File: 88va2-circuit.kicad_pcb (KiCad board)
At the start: 4 copper layers, 380 x 237.5 mm, 52 parts, among them CN2 FDD, CN4 TEXT BUS, CN5 LED, IC1 D65101GD055, IC13 SN74ALS374N, IC20 7407, IC21 uPD4990AC, IC22 DIP-14_W7.62mm, IC65 D65101GD110, IC8 SN74ALS374N, IC9 D65200GD076, X2 32.768K

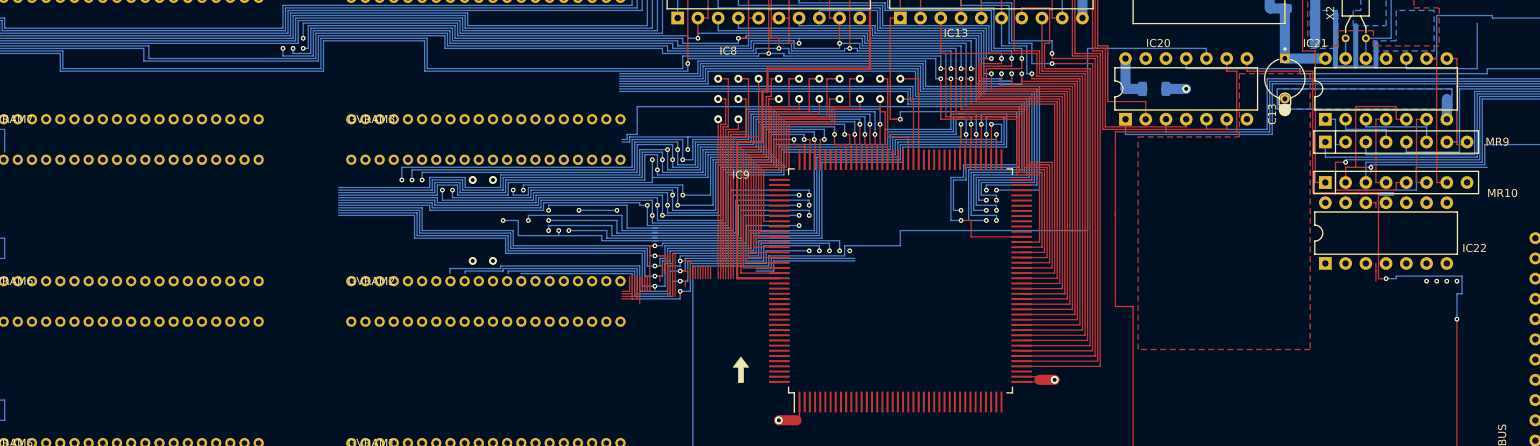
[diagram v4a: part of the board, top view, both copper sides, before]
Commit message: pcb: wire IC9 to GVRAM GA1x
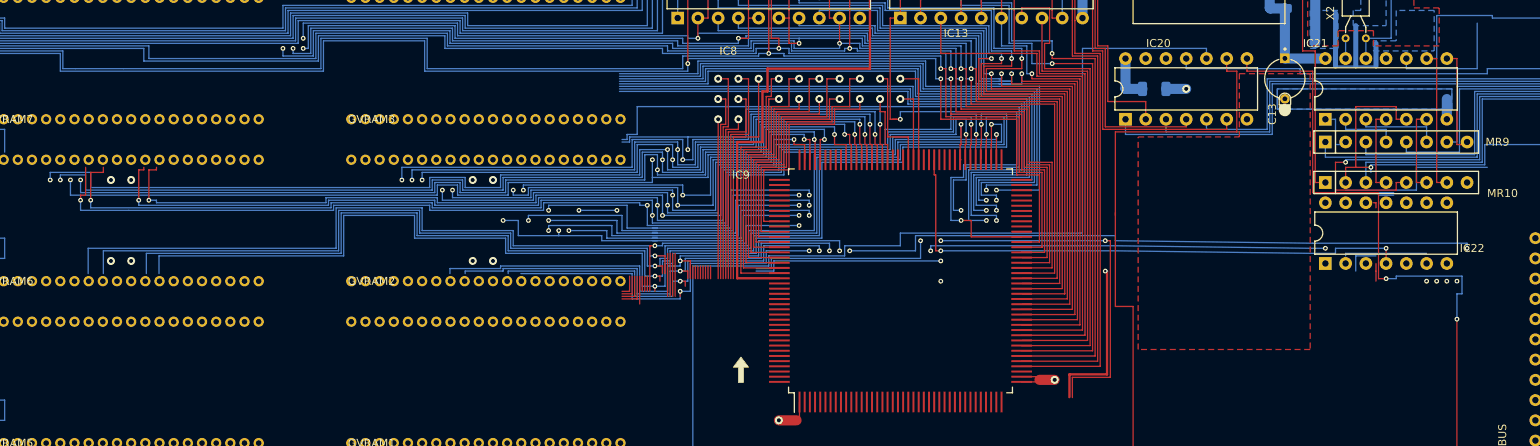
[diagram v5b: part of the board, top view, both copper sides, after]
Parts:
- IC22: value DIP-14_W7.62mm -> SN74LS74N
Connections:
- CN4 pad C1: unconnected-(CN4-??-PadC1) -> (no net)
- CN4 pad C13: (no net) -> GSCLK
- CN4 pad C24: (no net) -> IC9_90
- GVRAM1 pad 39: unconnected-(GVRAM1-~{SOE}-Pad39) -> XSOE
- GVRAM1 pad 40: unconnected-(GVRAM1-~{SEN}-Pad40) -> XSEN1
- GVRAM2 pad 39: unconnected-(GVRAM2-~{SOE}-Pad39) -> XSOE
- GVRAM2 pad 40: unconnected-(GVRAM2-~{SEN}-Pad40) -> XSEN1
- GVRAM3 pad 39: unconnected-(GVRAM3-~{SOE}-Pad39) -> XSOE
- GVRAM3 pad 40: unconnected-(GVRAM3-~{SEN}-Pad40) -> XSEN1
- GVRAM4 pad 39: unconnected-(GVRAM4-~{SOE}-Pad39) -> XSOE
- GVRAM4 pad 40: unconnected-(GVRAM4-~{SEN}-Pad40) -> XSEN1
- GVRAM5 pad 12: unconnected-(GVRAM5-A2-Pad12) -> GA12
- GVRAM5 pad 13: unconnected-(GVRAM5-A3-Pad13) -> GA13
- GVRAM5 pad 14: unconnected-(GVRAM5-~{RAS}-Pad14) -> XGRAS11
- GVRAM5 pad 15: unconnected-(GVRAM5-~{DT}/~{OE}-Pad15) -> XDTOE2
- GVRAM5 pad 26: unconnected-(GVRAM5-~{WE}/~{ME}-Pad26) -> XGWE2
- GVRAM5 pad 27: unconnected-(GVRAM5-~{CAS}-Pad27) -> XGCAS1
- GVRAM5 pad 28: unconnected-(GVRAM5-A4-Pad28) -> GA14
- GVRAM5 pad 29: unconnected-(GVRAM5-A5-Pad29) -> GA15
- GVRAM5 pad 32: unconnected-(GVRAM5-A6-Pad32) -> GA16
- GVRAM5 pad 33: unconnected-(GVRAM5-A7-Pad33) -> GA17
- GVRAM5 pad 39: unconnected-(GVRAM5-~{SOE}-Pad39) -> XSOE
- GVRAM5 pad 40: unconnected-(GVRAM5-~{SEN}-Pad40) -> XSEN2
- GVRAM5 pad 8: unconnected-(GVRAM5-A0-Pad8) -> GA10
- GVRAM5 pad 9: unconnected-(GVRAM5-A1-Pad9) -> GA11
- GVRAM6 pad 12: unconnected-(GVRAM6-A2-Pad12) -> GA12
- GVRAM6 pad 13: unconnected-(GVRAM6-A3-Pad13) -> GA13
- GVRAM6 pad 14: unconnected-(GVRAM6-~{RAS}-Pad14) -> XGRAS11
- GVRAM6 pad 15: unconnected-(GVRAM6-~{DT}/~{OE}-Pad15) -> XDTOE2
- GVRAM6 pad 26: unconnected-(GVRAM6-~{WE}/~{ME}-Pad26) -> XGWE2
- GVRAM6 pad 27: unconnected-(GVRAM6-~{CAS}-Pad27) -> XGCAS1
- GVRAM6 pad 28: unconnected-(GVRAM6-A4-Pad28) -> GA14
- GVRAM6 pad 29: unconnected-(GVRAM6-A5-Pad29) -> GA15
- GVRAM6 pad 32: unconnected-(GVRAM6-A6-Pad32) -> GA16
- GVRAM6 pad 33: unconnected-(GVRAM6-A7-Pad33) -> GA17
- GVRAM6 pad 39: unconnected-(GVRAM6-~{SOE}-Pad39) -> XSOE
- GVRAM6 pad 40: unconnected-(GVRAM6-~{SEN}-Pad40) -> XSEN2
- GVRAM6 pad 8: unconnected-(GVRAM6-A0-Pad8) -> GA10
- GVRAM6 pad 9: unconnected-(GVRAM6-A1-Pad9) -> GA11
- GVRAM7 pad 12: unconnected-(GVRAM7-A2-Pad12) -> GA12
- GVRAM7 pad 13: unconnected-(GVRAM7-A3-Pad13) -> GA13
- GVRAM7 pad 14: unconnected-(GVRAM7-~{RAS}-Pad14) -> XGRAS11
- GVRAM7 pad 15: unconnected-(GVRAM7-~{DT}/~{OE}-Pad15) -> XDTOE3
- GVRAM7 pad 26: unconnected-(GVRAM7-~{WE}/~{ME}-Pad26) -> XGWE3
- GVRAM7 pad 27: unconnected-(GVRAM7-~{CAS}-Pad27) -> XGCAS1
- GVRAM7 pad 28: unconnected-(GVRAM7-A4-Pad28) -> GA14
- GVRAM7 pad 29: unconnected-(GVRAM7-A5-Pad29) -> GA15
- GVRAM7 pad 32: unconnected-(GVRAM7-A6-Pad32) -> GA16
- GVRAM7 pad 33: unconnected-(GVRAM7-A7-Pad33) -> GA17
- GVRAM7 pad 39: unconnected-(GVRAM7-~{SOE}-Pad39) -> XSOE
- GVRAM7 pad 40: unconnected-(GVRAM7-~{SEN}-Pad40) -> XSEN2
- GVRAM7 pad 8: unconnected-(GVRAM7-A0-Pad8) -> GA10
- GVRAM7 pad 9: unconnected-(GVRAM7-A1-Pad9) -> GA11
- GVRAM8 pad 12: unconnected-(GVRAM8-A2-Pad12) -> GA12
- GVRAM8 pad 13: unconnected-(GVRAM8-A3-Pad13) -> GA13
- GVRAM8 pad 14: unconnected-(GVRAM8-~{RAS}-Pad14) -> XGRAS11
- GVRAM8 pad 15: unconnected-(GVRAM8-~{DT}/~{OE}-Pad15) -> XDTOE3
- GVRAM8 pad 26: unconnected-(GVRAM8-~{WE}/~{ME}-Pad26) -> XGWE3
- GVRAM8 pad 27: unconnected-(GVRAM8-~{CAS}-Pad27) -> XGCAS1
- GVRAM8 pad 28: unconnected-(GVRAM8-A4-Pad28) -> GA14
- GVRAM8 pad 29: unconnected-(GVRAM8-A5-Pad29) -> GA15
- GVRAM8 pad 32: unconnected-(GVRAM8-A6-Pad32) -> GA16
- GVRAM8 pad 33: unconnected-(GVRAM8-A7-Pad33) -> GA17
- GVRAM8 pad 39: unconnected-(GVRAM8-~{SOE}-Pad39) -> XSOE
- GVRAM8 pad 40: unconnected-(GVRAM8-~{SEN}-Pad40) -> XSEN2
- GVRAM8 pad 8: unconnected-(GVRAM8-A0-Pad8) -> GA10
- GVRAM8 pad 9: unconnected-(GVRAM8-A1-Pad9) -> GA11
- IC22 pad 1: (no net) -> unconnected-(IC22A-~{R}-Pad1)
- IC22 pad 2: (no net) -> unconnected-(IC22A-D-Pad2)
- IC22 pad 3: (no net) -> unconnected-(IC22A-C-Pad3)
- IC22 pad 4: (no net) -> Net-(IC22A-~{S})
- IC22 pad 5: (no net) -> unconnected-(IC22A-Q-Pad5)
- IC22 pad 6: (no net) -> unconnected-(IC22A-~{Q}-Pad6)
- IC9 pad 112: (no net) -> unconnected-(IC9-GA00-Pad112)
- IC9 pad 113: (no net) -> unconnected-(IC9-GA01-Pad113)
- IC9 pad 114: (no net) -> unconnected-(IC9-GA02-Pad114)
- IC9 pad 115: (no net) -> unconnected-(IC9-GA03-Pad115)
- IC9 pad 116: (no net) -> unconnected-(IC9-GA04-Pad116)
- IC9 pad 117: (no net) -> unconnected-(IC9-GA05-Pad117)
- IC9 pad 118: (no net) -> unconnected-(IC9-GA06-Pad118)
- IC9 pad 119: (no net) -> unconnected-(IC9-GA07-Pad119)
- IC9 pad 123: (no net) -> unconnected-(IC9-XGRAS0-Pad123)
- IC9 pad 124: (no net) -> unconnected-(IC9-XGCAS0-Pad124)
- IC9 pad 125: (no net) -> unconnected-(IC9-XGWE0-Pad125)
- IC9 pad 126: (no net) -> unconnected-(IC9-XGWE1-Pad126)
- IC9 pad 127: (no net) -> unconnected-(IC9-XDT0-Pad127)
- IC9 pad 128: (no net) -> unconnected-(IC9-XDT1-Pad128)
- IC9 pad 130: (no net) -> unconnected-(IC9-GDRQ0-Pad130)
- IC9 pad 155: (no net) -> unconnected-(IC9-XG0BLK-Pad155)
- IC9 pad 156: (no net) -> unconnected-(IC9-XG1BLK-Pad156)
- IC9 pad 43: (no net) -> GSCLK
- IC9 pad 70: (no net) -> XSOE
- IC9 pad 71: (no net) -> XSEN1
- IC9 pad 72: (no net) -> XSEN2
- IC9 pad 73: (no net) -> XDTOE2
- IC9 pad 74: (no net) -> XDTOE3
- IC9 pad 75: (no net) -> XGWE2
- IC9 pad 76: (no net) -> XGWE3
- IC9 pad 77: (no net) -> XGCAS1
- IC9 pad 78: (no net) -> XGRAS11
- IC9 pad 82: (no net) -> GA10
- IC9 pad 83: (no net) -> GA11
- IC9 pad 84: (no net) -> GA12
- IC9 pad 85: (no net) -> GA13
- IC9 pad 86: (no net) -> GA14
- IC9 pad 87: (no net) -> GA15
- IC9 pad 88: (no net) -> GA16
- IC9 pad 89: (no net) -> GA17
- IC9 pad 90: (no net) -> IC9_90
- IC9 pad 94: (no net) -> Net-(IC22A-~{S})
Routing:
- net (no net): track 5921.5 -> 5192.5 mm, vias 122 -> 111
- net GA13: track 0.00 -> 153.7 mm, vias 0 -> 2
- net GA11: track 0.00 -> 153.0 mm, vias 0 -> 2
- net GA12: track 0.00 -> 152.1 mm, vias 0 -> 2
- net GA10: track 0.00 -> 150.2 mm, vias 0 -> 2
- net GA16: track 0.00 -> 139.8 mm, vias 0 -> 3
- net GA17: track 0.00 -> 139.0 mm, vias 0 -> 3
- net GA15: track 0.00 -> 133.4 mm, vias 0 -> 3
- net GA14: track 0.00 -> 132.5 mm, vias 0 -> 3
- net Net-(IC22A-~{S}): track 0.00 -> 70.7 mm, vias 0 -> 2
- net unconnected-(IC9-GA06-Pad118): track 0.00 -> 62.0 mm, vias 0 -> 3
- net unconnected-(IC9-GA07-Pad119): track 0.00 -> 62.0 mm, vias 0 -> 3
- net unconnected-(IC9-GA05-Pad117): track 0.00 -> 54.4 mm, vias 0 -> 3
- net unconnected-(IC9-GA04-Pad116): track 0.00 -> 52.3 mm, vias 0 -> 3

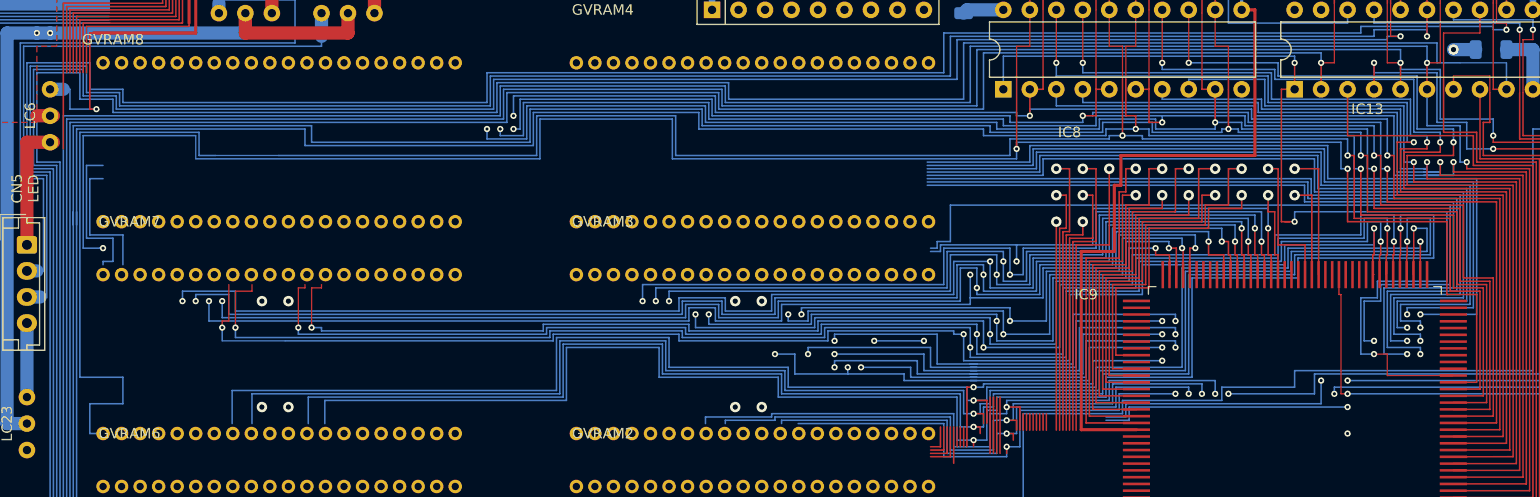
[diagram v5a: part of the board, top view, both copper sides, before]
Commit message: pcb: wire IC9 to GVRAM
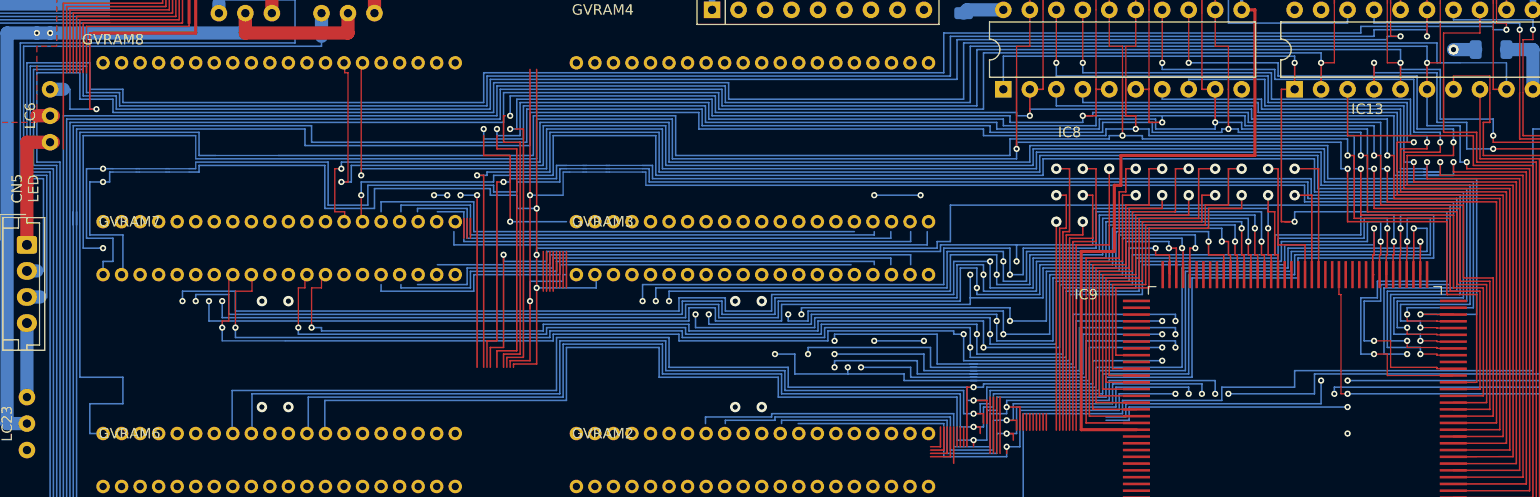
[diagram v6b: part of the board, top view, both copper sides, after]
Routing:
- net XSOE: track 0.00 -> 227.2 mm, vias 0 -> 5
- net XSEN2: track 0.00 -> 185.5 mm, vias 0 -> 2
- net XGCAS1: track 0.00 -> 159.1 mm, vias 0 -> 2
- net XGWE3: track 0.00 -> 155.7 mm, vias 0 -> 2
- net XGWE2: track 0.00 -> 152.8 mm, vias 0 -> 2
- net XGRAS11: track 0.00 -> 150.2 mm, vias 0 -> 2
- net XDTOE3: track 0.00 -> 149.3 mm, vias 0 -> 2
- net XDTOE2: track 0.00 -> 143.0 mm, vias 0 -> 2
- net (no net): track 5192.5 -> 5273.2 mm, vias 111 -> 113
- net GA17: track 139.0 -> 140.1 mm
- net GA14: track 132.5 -> 133.6 mm
- net GA15: track 133.4 -> 134.5 mm
- net GA12: track 152.1 -> 153.1 mm
- net GA16: track 139.8 -> 140.8 mm
- net GA13: track 153.7 -> 154.7 mm
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
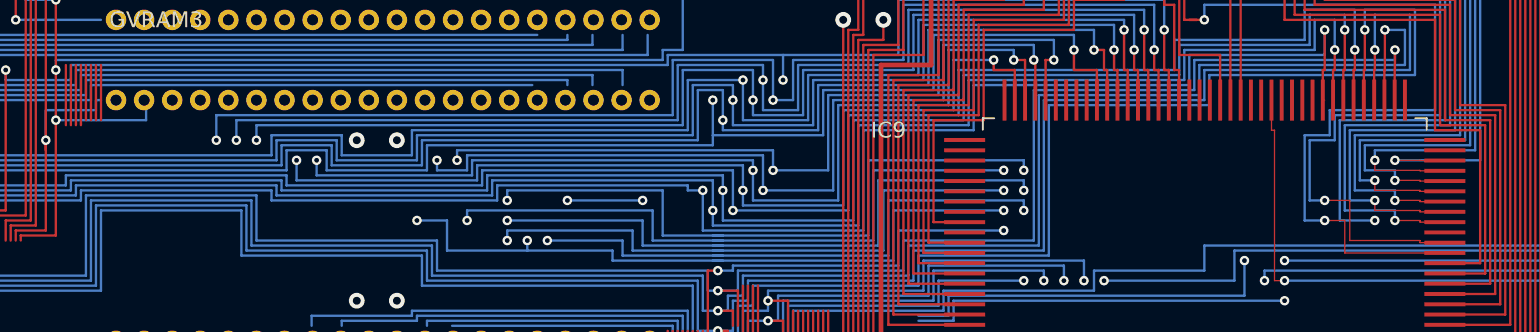
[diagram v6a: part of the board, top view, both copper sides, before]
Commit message: pcb: wire IC9 to GVRAM
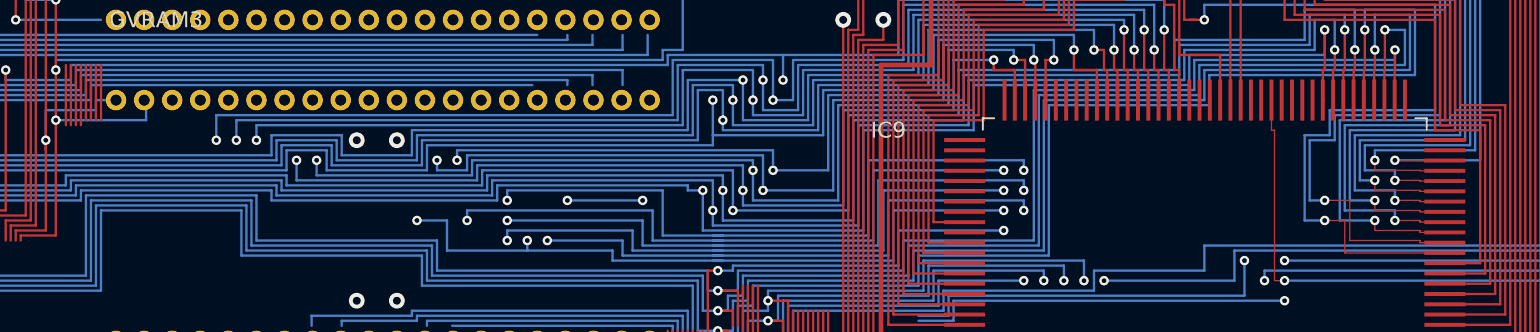
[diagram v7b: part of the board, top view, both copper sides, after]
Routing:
- net XSEN1: track 0.00 -> 160.4 mm, vias 0 -> 3
- net (no net): track 5273.2 -> 5118.9 mm, vias 113 -> 110

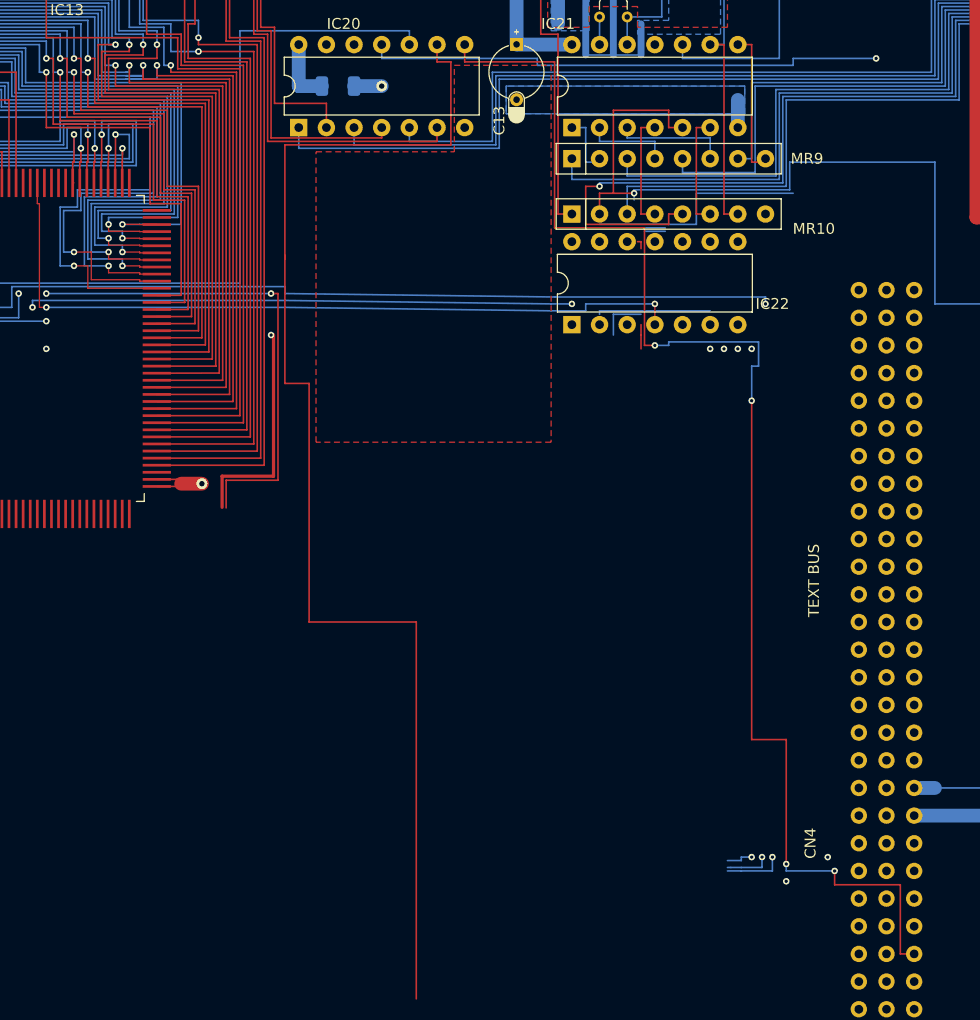
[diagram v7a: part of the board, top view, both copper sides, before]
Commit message: pcb: wire IC9 pin 43 and 90. schematic: fix TEXT BUS
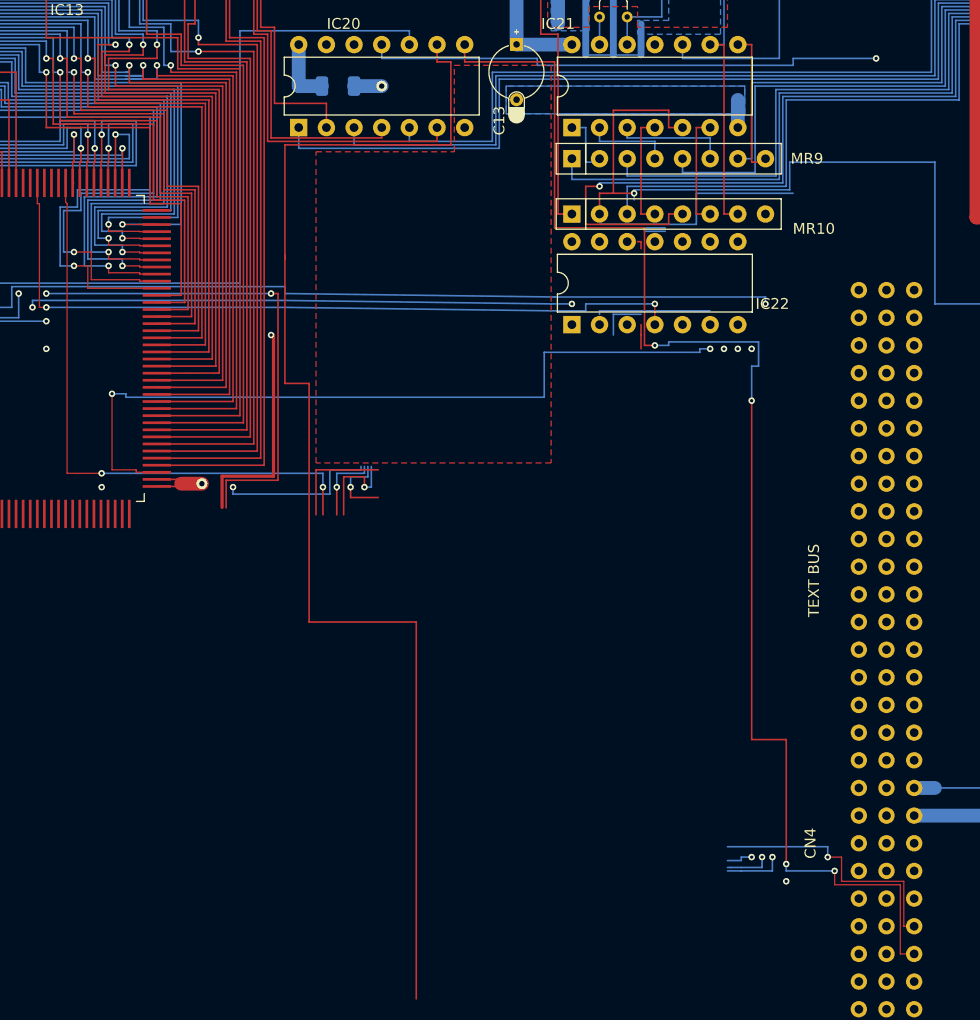
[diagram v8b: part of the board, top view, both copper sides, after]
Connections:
- CN4 pad C13: GSCLK -> (no net)
- CN4 pad C18: (no net) -> GSCLK
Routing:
- net IC9_90: track 0.00 -> 78.5 mm, vias 0 -> 3
- net GSCLK: track 0.00 -> 71.0 mm, vias 0 -> 2
- net (no net): track 5118.9 -> 5166.5 mm, vias 110 -> 113
